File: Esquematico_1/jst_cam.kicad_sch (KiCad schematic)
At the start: 19 parts, among them J1 Screw_Terminal_01x04, J2 Screw_Terminal_01x03, J3 Screw_Terminal_01x06, J4 Screw_Terminal_01x08, J6 Screw_Terminal_01x05, J7 USB_C_Receptacle_USB2.0_16P, U5 USBLC6-2SC6

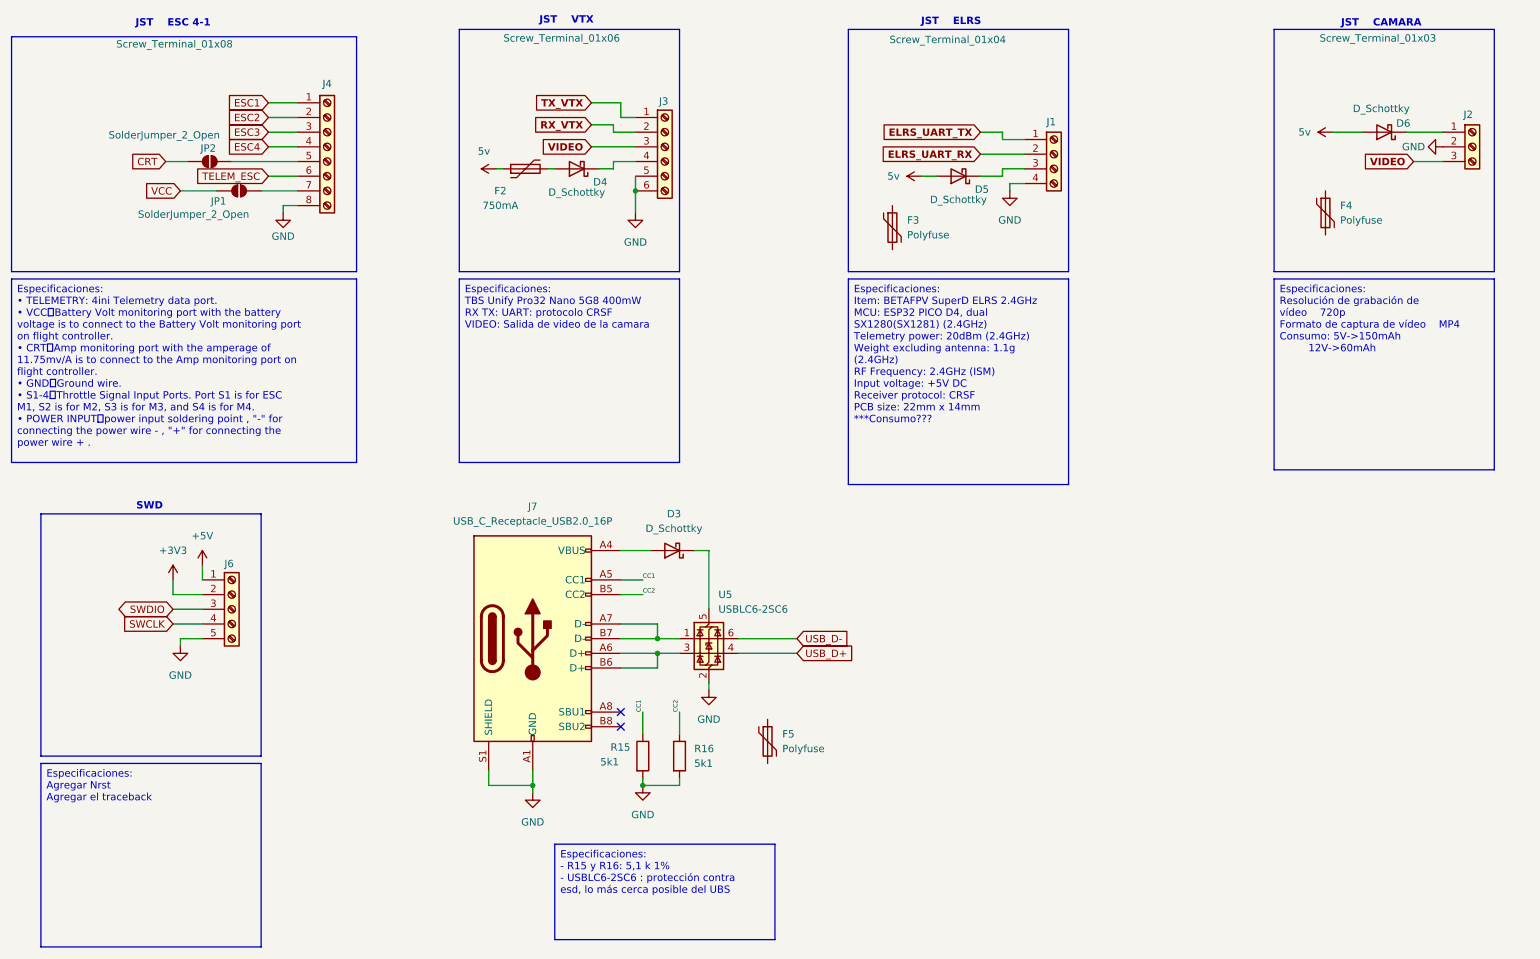
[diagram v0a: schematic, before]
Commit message: LDS y gran corrección de errores del esquemático
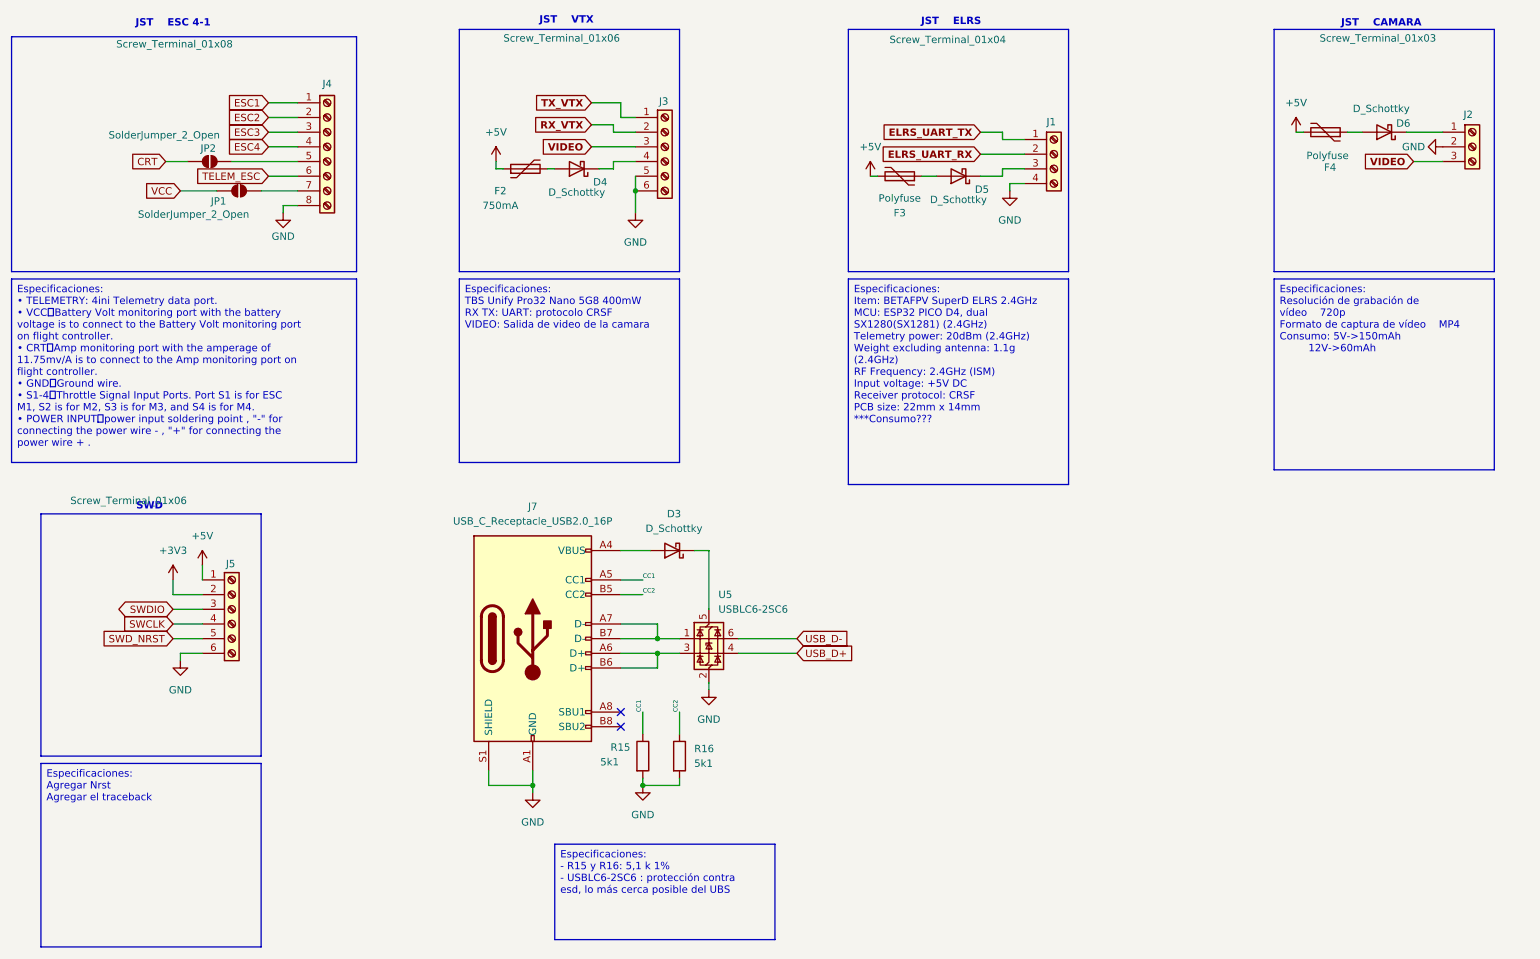
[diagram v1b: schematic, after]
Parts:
- removed F5: Polyfuse, symbol Device:Polyfuse
- removed J6: Screw_Terminal_01x05, symbol Connector:Screw_Terminal_01x05
- added J5: Screw_Terminal_01x06, symbol Connector:Screw_Terminal_01x06
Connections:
- net +3V3: now also J5.2 (Pin_2)
- net +5V: now also F2.1, F3.2, F4.2, J5.1 (Pin_1)
- net GND: now also J5.6 (Pin_6)
- net SWCLK: now also J5.4 (Pin_4)
- net SWDIO: now also J5.3 (Pin_3)
- net at F4.1: now also D6.2 (A)
- net at F3.1: now also D5.2 (A)
- removed net 5v: D5.2 (A), D6.2 (A), F2.1
- new net SWD_NRST: J5.5 (Pin_5)
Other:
- moved on the sheet: F3, F4

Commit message: Todos los footprints menos ESC
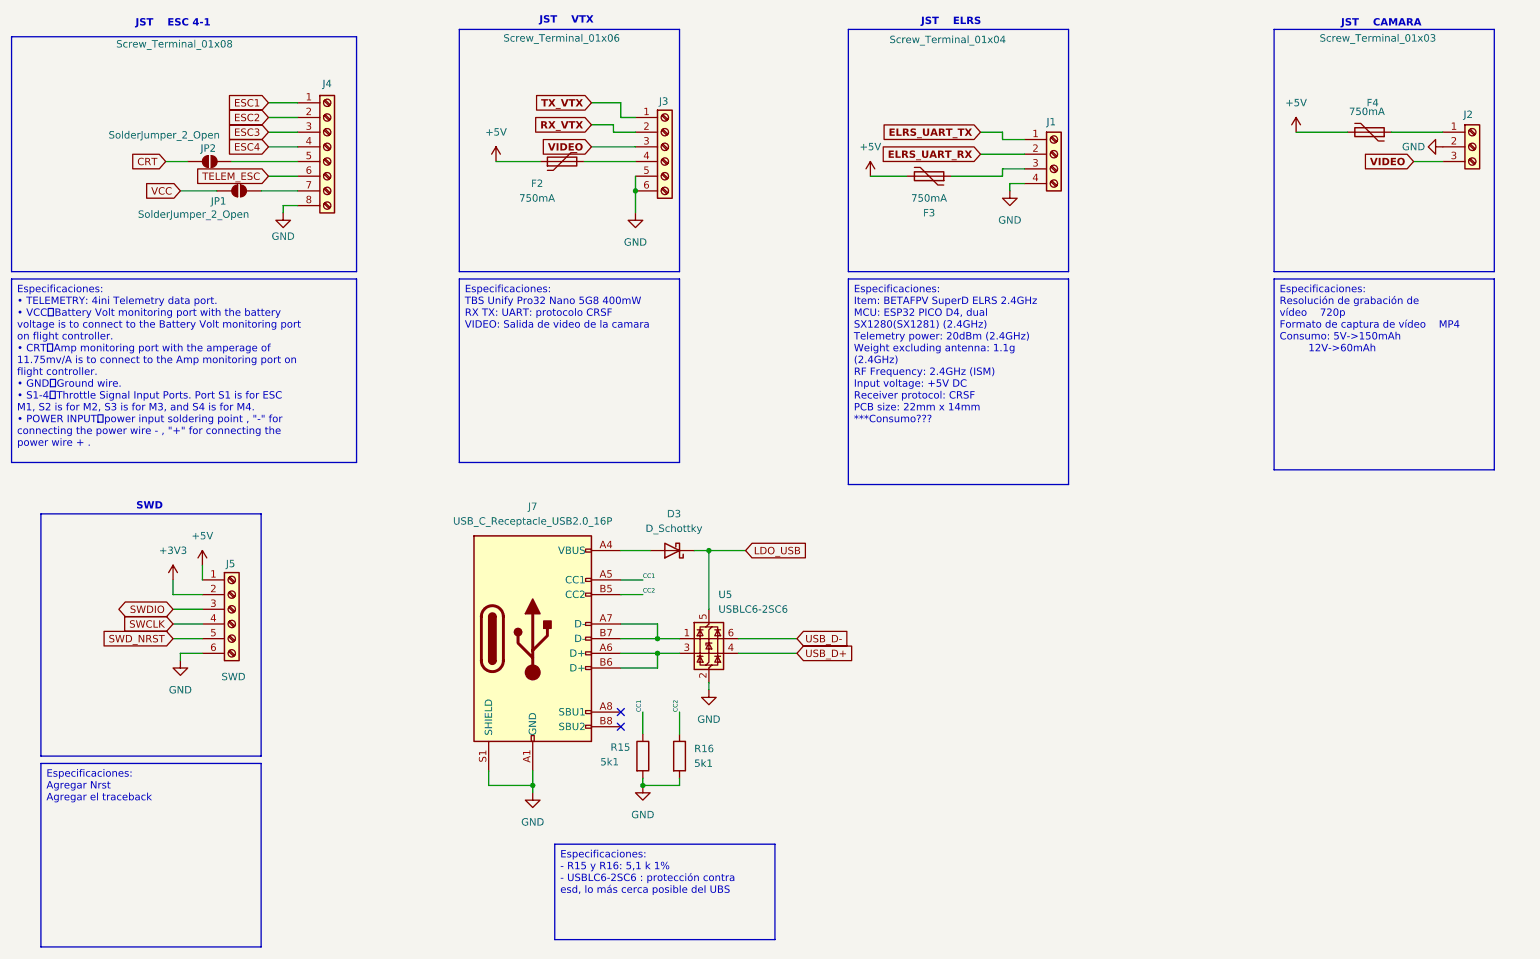
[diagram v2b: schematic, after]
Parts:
- removed D4, D5, D6: D_Schottky, Package_TO_SOT_SMD:SOT-23, symbol Device:D_Schottky
- F3, F4: value Polyfuse -> 750mA; footprint (none) -> Capacitor_SMD:C_0805_2012Metric_Pad1.18x1.45mm_HandSolder
- J5: value Screw_Terminal_01x06 -> SWD; footprint (none) -> Connector_PinHeader_1.00mm:PinHeader_1x06_P1.00mm_Vertical_SMD_Pin1Left
- J7: footprint (none) -> USB4940-00-A:USB494000A
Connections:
- net at J1.3 (Pin_3): now also F3.1
- net at F4.1: now also J2.1 (Pin_1)
- net at J3.4 (Pin_4): now also F2.2
- net LDO_USB: now reaches D3.1 (K), U5.5 (VBUS)
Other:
- moved on the sheet: F2, F3, F4

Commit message: Update PCB y JST
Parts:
- J1: footprint (none) -> Connector_JST:JST_SH_SM04B-SRSS-TB_1x04-1MP_P1.00mm_Horizontal
- J2: footprint (none) -> Connector_JST:JST_SH_SM03B-SRSS-TB_1x03-1MP_P1.00mm_Horizontal
- J3: footprint (none) -> Connector_JST:JST_SH_SM06B-SRSS-TB_1x06-1MP_P1.00mm_Horizontal
- J4: footprint (none) -> Connector_JST:JST_SH_SM08B-SRSS-TB_1x08-1MP_P1.00mm_Horizontal
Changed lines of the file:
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@@
 			)
 		)
-		(property "Footprint" ""
+		(property "Footprint" "Connector_JST:JST_SH_SM03B-SRSS-TB_1x03-1MP_P1.00mm_Horizontal"
 			(at 271.78 43.18 0)
 			(effects
@@
 			)
 		)
-		(property "Footprint" ""
+		(property "Footprint" "Connector_JST:JST_SH_SM06B-SRSS-TB_1x06-1MP_P1.00mm_Horizontal"
 			(at 132.08 43.18 0)
 			(effects
@@
 			)
 		)
-		(property "Footprint" ""
+		(property "Footprint" "Connector_JST:JST_SH_SM04B-SRSS-TB_1x04-1MP_P1.00mm_Horizontal"
 			(at 199.39 44.45 0)
 			(effects
@@
 			)
 		)
-		(property "Footprint" ""
+		(property "Footprint" "Connector_JST:JST_SH_SM08B-SRSS-TB_1x08-1MP_P1.00mm_Horizontal"
 			(at 73.66 43.18 0)
 			(effects

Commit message: BIG Update conexionado MCU y PCB
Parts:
- added F5: 750mA, Capacitor_SMD:C_0805_2012Metric_Pad1.18x1.45mm_HandSolder, symbol Device:Polyfuse
- added J6: Screw_Terminal_01x04, Connector_JST:JST_SH_SM04B-SRSS-TB_1x04-1MP_P1.00mm_Horizontal, symbol Connector:Screw_Terminal_01x04
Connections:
- net +3V3: now also F5.2
- net GND: now also J6.4 (Pin_4)
- new net: F5.1, J6.3 (Pin_3)
- new net GPS_UART_RX: J6.2 (Pin_2)
- new net GPS_UART_TX: J6.1 (Pin_1)
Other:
- note added: "JST GPS"
- moved on the sheet: F3, F4, J1, J2

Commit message: Update PCB backlayer
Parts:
- added J8: Screw_Terminal_01x02, TerminalBlock:TerminalBlock_Xinya_XY308-2.54-2P_1x02_P2.54mm_Horizontal, symbol Connector:Screw_Terminal_01x02
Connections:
- net GND: now also J8.2 (Pin_2)
- new net Vbat: J8.1 (Pin_1)
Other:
- note added: "JST POWER"
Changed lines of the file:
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@@
+		)
+	)
+	(text "JST	POWER\n\n\n"
+		(exclude_from_sim no)
+		(at 208.026 116.84 0)
+		(effects
+			(font
+				(size 1.27 1.27)
+				(thickness 0.254)
+				(bold yes)
+			)
 		)
 	)
@@
 	(wire
 		(pts
+			(xy 205.74 125.73) (xy 209.55 125.73)
+		)
+		(stroke
+			(width 0)
+			(type default)
+		)
+	)
+	(wire
+		(pts
 			(xy 157.48 48.26) (xy 166.37 48.26)
 		)
@@
 		(pts
 			(xy 250.19 44.45) (xy 257.81 44.45)
+		)
+		(stroke
+			(width 0)
+			(type default)
+		)
+	)
+	(wire
+		(pts
+			(xy 203.2 123.19) (xy 209.55 123.19)
 		)
 		(stroke
@@
 				)
 				(justify left)
+				(hide yes)
+			)
+		)
+	)
+	(global_label "Vbat"
+		(shape input)
+		(at 203.2 123.19 180)
+		(fields_autoplaced yes)
+		(effects
+			(font
+				(size 1.27 1.27)
+			)
+			(justify right)
+		)
+		(property "Intersheetrefs" "${INTERSHEET_REFS}"
+			(at 196.1025 123.19 0)
+			(effects
+				(font
+					(size 1.27 1.27)
+				)
+				(justify right)
 				(hide yes)
 			)
@@
 	)
 	(symbol
+		(lib_id "power:GND")
+		(at 205.74 125.73 0)
+		(unit 1)
+		(exclude_from_sim no)
+		(in_bom yes)
+		(on_board yes)
+		(dnp no)
+		(fields_autoplaced yes)
+		(property "Reference" "#PWR055"
+			(at 205.74 132.08 0)
+			(effects
+				(font
+					(size 1.27 1.27)
+				)
+				(hide yes)
+			)
+		)
+		(property "Value" "GND"
+			(at 205.74 130.81 0)
+			(effects
+				(font
+					(size 1.27 1.27)
+				)
+			)
+		)
+		(property "Footprint" ""
+			(at 205.74 125.73 0)
+			(effects
+				(font
+					(size 1.27 1.27)
+				)
+				(hide yes)
+			)
+		)
+		(property "Datasheet" ""
+			(at 205.74 125.73 0)
+			(effects
+				(font
+					(size 1.27 1.27)
+				)
+				(hide yes)
+			)
+		)
+		(property "Description" "Power symbol creates a global label with name \"GND\" , ground"
+			(at 205.74 125.73 0)
+			(effects
+				(font
+					(size 1.27 1.27)
+				)
+				(hide yes)
+			)
+		)
+		(pin "1"
+		)
+		(instances
+			(project "Esquematico_1"
+				(path "/de2d80c1-c21c-478d-b724-17659b714c38/457e76de-adfe-4ec5-a818-c5970caa89a7"
+					(reference "#PWR055")
+					(unit 1)
+				)
+			)
+		)
+	)
+	(symbol
 		(lib_id "Connector:Screw_Terminal_01x06")
 		(at 57.15 123.19 0)
@@
 					(unit 1)
 				)
+			)
+		)
+	)
+	(symbol
+		(lib_id "Connector:Screw_Terminal_01x02")
+		(at 214.63 123.19 0)
+		(unit 1)
+		(exclude_from_sim no)
+		(in_bom yes)
+		(on_board yes)
+		(dnp no)
+		(property "Reference" "J8"
+			(at 213.36 120.396 0)
+			(effects
+				(font
+					(size 1.27 1.27)
+				)
+				(justify left)
+			)
+		)
+		(property "Value" "Screw_Terminal_01x02"
+			(at 198.374 117.348 0)
+			(effects
+				(font
+					(size 1.27 1.27)
+				)
+				(justify left)
+			)
+		)
+		(property "Footprint" "TerminalBlock:TerminalBlock_Xinya_XY308-2.54-2P_1x02_P2.54mm_Horizontal"
+			(at 214.63 123.19 0)
+			(effects
+				(font
+					(size 1.27 1.27)
+				)
+				(hide yes)
+			)
+		)
+		(property "Datasheet" "~"
+			(at 214.63 123.19 0)
+			(effects
+				(font
+					(size 1.27 1.27)
+				)
+				(hide yes)
+			)
+		)
+		(property "Description" "Generic screw terminal, single row, 01x02, script generated (kicad-library-utils/schlib/autogen/connector/)"
+			(at 214.63 123.19 0)
+			(effects
+				(font
+					(size 1.27 1.27)
+				)
+				(hide yes)
+			)
+		)
+		(pin "2"
+		)
+		(pin "1"
+		)
+		(instances
+			(project ""
+				(path "/de2d80c1-c21c-478d-b724-17659b714c38/457e76de-adfe-4ec5-a818-c5970caa89a7"
+					(reference "J8")
+					(unit 1)
+				)

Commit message: Update arreglo de errores
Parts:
- removed J8: Screw_Terminal_01x02, TerminalBlock:TerminalBlock_Xinya_XY308-2.54-2P_1x02_P2.54mm_Horizontal, symbol Connector:Screw_Terminal_01x02
- added J8, J9: Screw_Terminal_01x01, TestPoint:TestPoint_Pad_2.5x2.5mm, symbol Connector:Screw_Terminal_01x01
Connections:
- net GND: now also J9.1 (Pin_1)
- net Vbat: now also J8.1 (Pin_1)
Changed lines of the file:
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@@
+	)
+	(symbol
+		(lib_id "Connector:Screw_Terminal_01x01")
+		(at 214.63 123.19 0)
+		(unit 1)
+		(exclude_from_sim no)
+		(in_bom yes)
+		(on_board yes)
+		(dnp no)
+		(fields_autoplaced yes)
+		(property "Reference" "J8"
+			(at 217.17 121.9199 0)
+			(effects
+				(font
+					(size 1.27 1.27)
+				)
+				(justify left)
+			)
+		)
+		(property "Value" "Screw_Terminal_01x01"
+			(at 217.17 124.4599 0)
+			(effects
+				(font
+					(size 1.27 1.27)
+				)
+				(justify left)
+			)
+		)
+		(property "Footprint" "TestPoint:TestPoint_Pad_2.5x2.5mm"
+			(at 214.63 123.19 0)
+			(effects
+				(font
+					(size 1.27 1.27)
+				)
+				(hide yes)
+			)
+		)
+		(property "Datasheet" "~"
+			(at 214.63 123.19 0)
+			(effects
+				(font
+					(size 1.27 1.27)
+				)
+				(hide yes)
+			)
+		)
+		(property "Description" "Generic screw terminal, single row, 01x01, script generated (kicad-library-utils/schlib/autogen/connector/)"
+			(at 214.63 123.19 0)
+			(effects
+				(font
+					(size 1.27 1.27)
+				)
+				(hide yes)
+			)
+		)
+		(pin "1"
+		)
+		(instances
+			(project ""
+				(path "/de2d80c1-c21c-478d-b724-17659b714c38/457e76de-adfe-4ec5-a818-c5970caa89a7"
+					(reference "J8")
+					(unit 1)
+				)
+			)
+		)
 	)
 	(symbol
@@
 	)
 	(symbol
-		(lib_id "Connector:Screw_Terminal_01x02")
-		(at 214.63 123.19 0)
-		(unit 1)
-		(exclude_from_sim no)
-		(in_bom yes)
-		(on_board yes)
-		(dnp no)
-		(property "Reference" "J8"
-			(at 213.36 120.396 0)
-			(effects
-				(font
-					(size 1.27 1.27)
-				)
-				(justify left)
-			)
-		)
-		(property "Value" "Screw_Terminal_01x02"
-			(at 198.374 117.348 0)
-			(effects
-				(font
-					(size 1.27 1.27)
-				)
-				(justify left)
-			)
-		)
-		(property "Footprint" "TerminalBlock:TerminalBlock_Xinya_XY308-2.54-2P_1x02_P2.54mm_Horizontal"
-			(at 214.63 123.19 0)
-			(effects
-				(font
-					(size 1.27 1.27)
-				)
-				(hide yes)
-			)
-		)
-		(property "Datasheet" "~"
-			(at 214.63 123.19 0)
-			(effects
-				(font
-					(size 1.27 1.27)
-				)
-				(hide yes)
-			)
-		)
-		(property "Description" "Generic screw terminal, single row, 01x02, script generated (kicad-library-utils/schlib/autogen/connector/)"
-			(at 214.63 123.19 0)
-			(effects
-				(font
-					(size 1.27 1.27)
-				)
-				(hide yes)
-			)
-		)
-		(pin "2"
-		)
-		(pin "1"
-		)
-		(instances
-			(project ""
-				(path "/de2d80c1-c21c-478d-b724-17659b714c38/457e76de-adfe-4ec5-a818-c5970caa89a7"
-					(reference "J8")
-					(unit 1)
-				)
-			)
-		)
-	)
-	(symbol
 		(lib_id "Power_Protection:USBLC6-2SC6")
 		(at 139.7 128.27 0)
@@
 					(unit 1)
 				)
+			)
+		)
+	)
+	(symbol
+		(lib_id "Connector:Screw_Terminal_01x01")
+		(at 214.63 125.73 0)
+		(unit 1)
+		(exclude_from_sim no)
+		(in_bom yes)
+		(on_board yes)
+		(dnp no)
+		(property "Reference" "J9"
+			(at 216.916 129.286 0)
+			(effects
+				(font
+					(size 1.27 1.27)
+				)
+				(justify left)
+			)
+		)
+		(property "Value" "Screw_Terminal_01x01"
+			(at 217.17 126.9999 0)
+			(effects
+				(font
+					(size 1.27 1.27)
+				)
+				(justify left)
+			)
+		)
+		(property "Footprint" "TestPoint:TestPoint_Pad_2.5x2.5mm"
+			(at 214.63 125.73 0)
+			(effects
+				(font
+					(size 1.27 1.27)
+				)
+				(hide yes)
+			)
+		)
+		(property "Datasheet" "~"
+			(at 214.63 125.73 0)
+			(effects
+				(font
+					(size 1.27 1.27)
+				)
+				(hide yes)
+			)
+		)
+		(property "Description" "Generic screw terminal, single row, 01x01, script generated (kicad-library-utils/schlib/autogen/connector/)"
+			(at 214.63 125.73 0)
+			(effects
+				(font
+					(size 1.27 1.27)
+				)
+				(hide yes)
+			)
+		)
+		(pin "1"
+		)
+		(instances
+			(project "Esquematico_1"
+				(path "/de2d80c1-c21c-478d-b724-17659b714c38/457e76de-adfe-4ec5-a818-c5970caa89a7"
+					(reference "J9")
+					(unit 1)
+				)
